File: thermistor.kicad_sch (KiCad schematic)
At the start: 5 parts, among them J15 Conn_01x02

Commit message: more layout and memes
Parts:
- C12: LibRef (none) -> CL10A105KA8NNNC; SKU (none) -> CL10A105KA8NNNC; Supplier (none) -> Digikey
- D12: value RED -> RED 0603; LibRef (none) -> B1911USD-20D000114U1930; SKU (none) -> B1911USD-20D000114U1930; Supplier (none) -> Digikey
- J15: value Conn_01x02 -> JST S2B-PH-SM4-TB; LibRef (none) -> S2B-PH-SM4-TB; SKU (none) -> S2B-PH-SM4-TB; Supplier (none) -> Digikey
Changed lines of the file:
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@@
       (effects (font (size 1.27 1.27)) (justify right))
     )
-    (property "Value" "RED" (at 80.01 87.9475 90)
+    (property "Value" "RED 0603" (at 80.01 87.9475 90)
       (effects (font (size 1.27 1.27)) (justify right))
     )
@@
     )
     (property "Datasheet" "~" (at 76.2 85.09 0)
+      (effects (font (size 1.27 1.27)) hide)
+    )
+    (property "LibRef" "B1911USD-20D000114U1930" (at 76.2 85.09 0)
+      (effects (font (size 1.27 1.27)) hide)
+    )
+    (property "SKU" "B1911USD-20D000114U1930" (at 76.2 85.09 0)
+      (effects (font (size 1.27 1.27)) hide)
+    )
+    (property "Supplier" "Digikey" (at 76.2 85.09 0)
       (effects (font (size 1.27 1.27)) hide)
     )
@@
       (effects (font (size 1.27 1.27)) hide)
     )
+    (property "LibRef" "CL10A105KA8NNNC" (at 119.38 90.17 0)
+      (effects (font (size 1.27 1.27)) hide)
+    )
+    (property "SKU" "CL10A105KA8NNNC" (at 119.38 90.17 0)
+      (effects (font (size 1.27 1.27)) hide)
+    )
+    (property "Supplier" "Digikey" (at 119.38 90.17 0)
+      (effects (font (size 1.27 1.27)) hide)
+    )
+    (property "Description" "CAP CER 1UF 25V X5R 0603" (at 119.38 90.17 0)
+      (effects (font (size 1.27 1.27)) hide)
+    )
     (pin "1")
     (pin "2")
@@
       (effects (font (size 1.27 1.27)) (justify left))
     )
-    (property "Value" "Conn_01x02" (at 138.43 87.63 0)
+    (property "Value" "JST S2B-PH-SM4-TB" (at 138.43 87.63 0)
       (effects (font (size 1.27 1.27)) (justify left))
     )
@@
     )
     (property "Datasheet" "~" (at 135.89 85.09 0)
+      (effects (font (size 1.27 1.27)) hide)
+    )
+    (property "LibRef" "S2B-PH-SM4-TB" (at 135.89 85.09 0)
+      (effects (font (size 1.27 1.27)) hide)
+    )
+    (property "SKU" "S2B-PH-SM4-TB" (at 135.89 85.09 0)
+      (effects (font (size 1.27 1.27)) hide)
+    )
+    (property "Supplier" "Digikey" (at 135.89 85.09 0)
       (effects (font (size 1.27 1.27)) hide)
     )
@@
       (effects (font (size 1.27 1.27)) hide)
     )
+    (property "LibRef" "" (at 119.38 74.93 0)
+      (effects (font (size 1.27 1.27)) hide)
+    )
+    (property "SKU" "" (at 119.38 74.93 0)
+      (effects (font (size 1.27 1.27)) hide)
+    )
+    (property "Supplier" "" (at 119.38 74.93 0)
+      (effects (font (size 1.27 1.27)) hide)
+    )
     (pin "1")
     (pin "2")
@@
       (effects (font (size 1.27 1.27)) hide)
     )
+    (property "LibRef" "" (at 76.2 77.47 0)
+      (effects (font (size 1.27 1.27)) hide)
+    )
+    (property "SKU" "" (at 76.2 77.47 0)
+      (effects (font (size 1.27 1.27)) hide)
+    )
+    (property "Supplier" "" (at 76.2 77.47 0)
+      (effects (font (size 1.27 1.27)) hide)
+    )

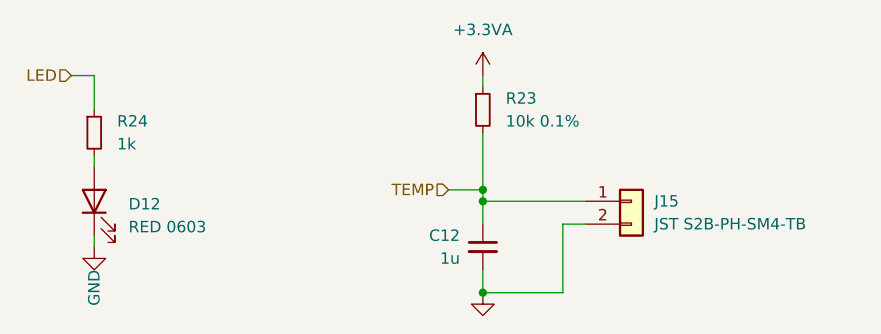
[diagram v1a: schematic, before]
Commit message: update firmware to do calibration and work with orion BMS
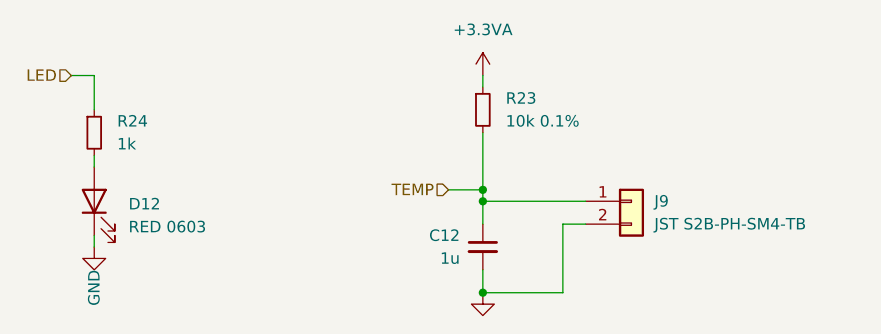
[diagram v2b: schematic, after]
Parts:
- renumbered J15 to J9
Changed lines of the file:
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@@
   (symbol (lib_id "power:GND") (at 119.38 95.25 0) (mirror y) (unit 1)
     (in_bom yes) (on_board yes) (dnp no)
-    (property "Reference" "#PWR03" (at 119.38 101.6 0)
+    (property "Reference" "#PWR036" (at 119.38 101.6 0)
       (effects (font (size 1.27 1.27)) hide)
     )
@@
     (instances
       (project "cell-tap-connector-pcb"
-        (path "/b8571e6a-e18a-40b9-808f-3f086437be1b"
-          (reference "#PWR03") (unit 1)
-        )
         (path "/b8571e6a-e18a-40b9-808f-3f086437be1b/fc85c946-576e-4f03-89ac-fa7b10888158/396ddede-e7b2-47c7-98e8-42b3988715ee"
           (reference "#PWR036") (unit 1)
@@
   (symbol (lib_id "Connector_Generic:Conn_01x02") (at 135.89 85.09 0) (unit 1)
     (in_bom yes) (on_board yes) (dnp no) (fields_autoplaced)
-    (property "Reference" "J15" (at 138.43 85.09 0)
+    (property "Reference" "J9" (at 138.43 85.09 0)
       (effects (font (size 1.27 1.27)) (justify left))
     )
@@
     (instances
       (project "cell-tap-connector-pcb"
-        (path "/b8571e6a-e18a-40b9-808f-3f086437be1b"
-          (reference "J15") (unit 1)
-        )
         (path "/b8571e6a-e18a-40b9-808f-3f086437be1b/fc85c946-576e-4f03-89ac-fa7b10888158/396ddede-e7b2-47c7-98e8-42b3988715ee"
           (reference "J9") (unit 1)
@@
   (symbol (lib_id "power:GND") (at 76.2 90.17 0) (mirror y) (unit 1)
     (in_bom yes) (on_board yes) (dnp no)
-    (property "Reference" "#PWR03" (at 76.2 96.52 0)
+    (property "Reference" "#PWR035" (at 76.2 96.52 0)
       (effects (font (size 1.27 1.27)) hide)
     )
@@
     (instances
       (project "cell-tap-connector-pcb"
-        (path "/b8571e6a-e18a-40b9-808f-3f086437be1b"
-          (reference "#PWR03") (unit 1)
-        )
         (path "/b8571e6a-e18a-40b9-808f-3f086437be1b/fc85c946-576e-4f03-89ac-fa7b10888158/396ddede-e7b2-47c7-98e8-42b3988715ee"
           (reference "#PWR035") (unit 1)

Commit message: Kicad Update
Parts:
- renumbered C12 to C3, D12 to D3, J9 to J1, R23 to R5, R24 to R6
